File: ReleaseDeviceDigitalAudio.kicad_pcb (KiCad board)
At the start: 2 copper layers, 132.1 x 67.9 mm, 2 parts, among them J3 Conn_02x15_Odd_Even, J9 Conn_02x08_Odd_Even

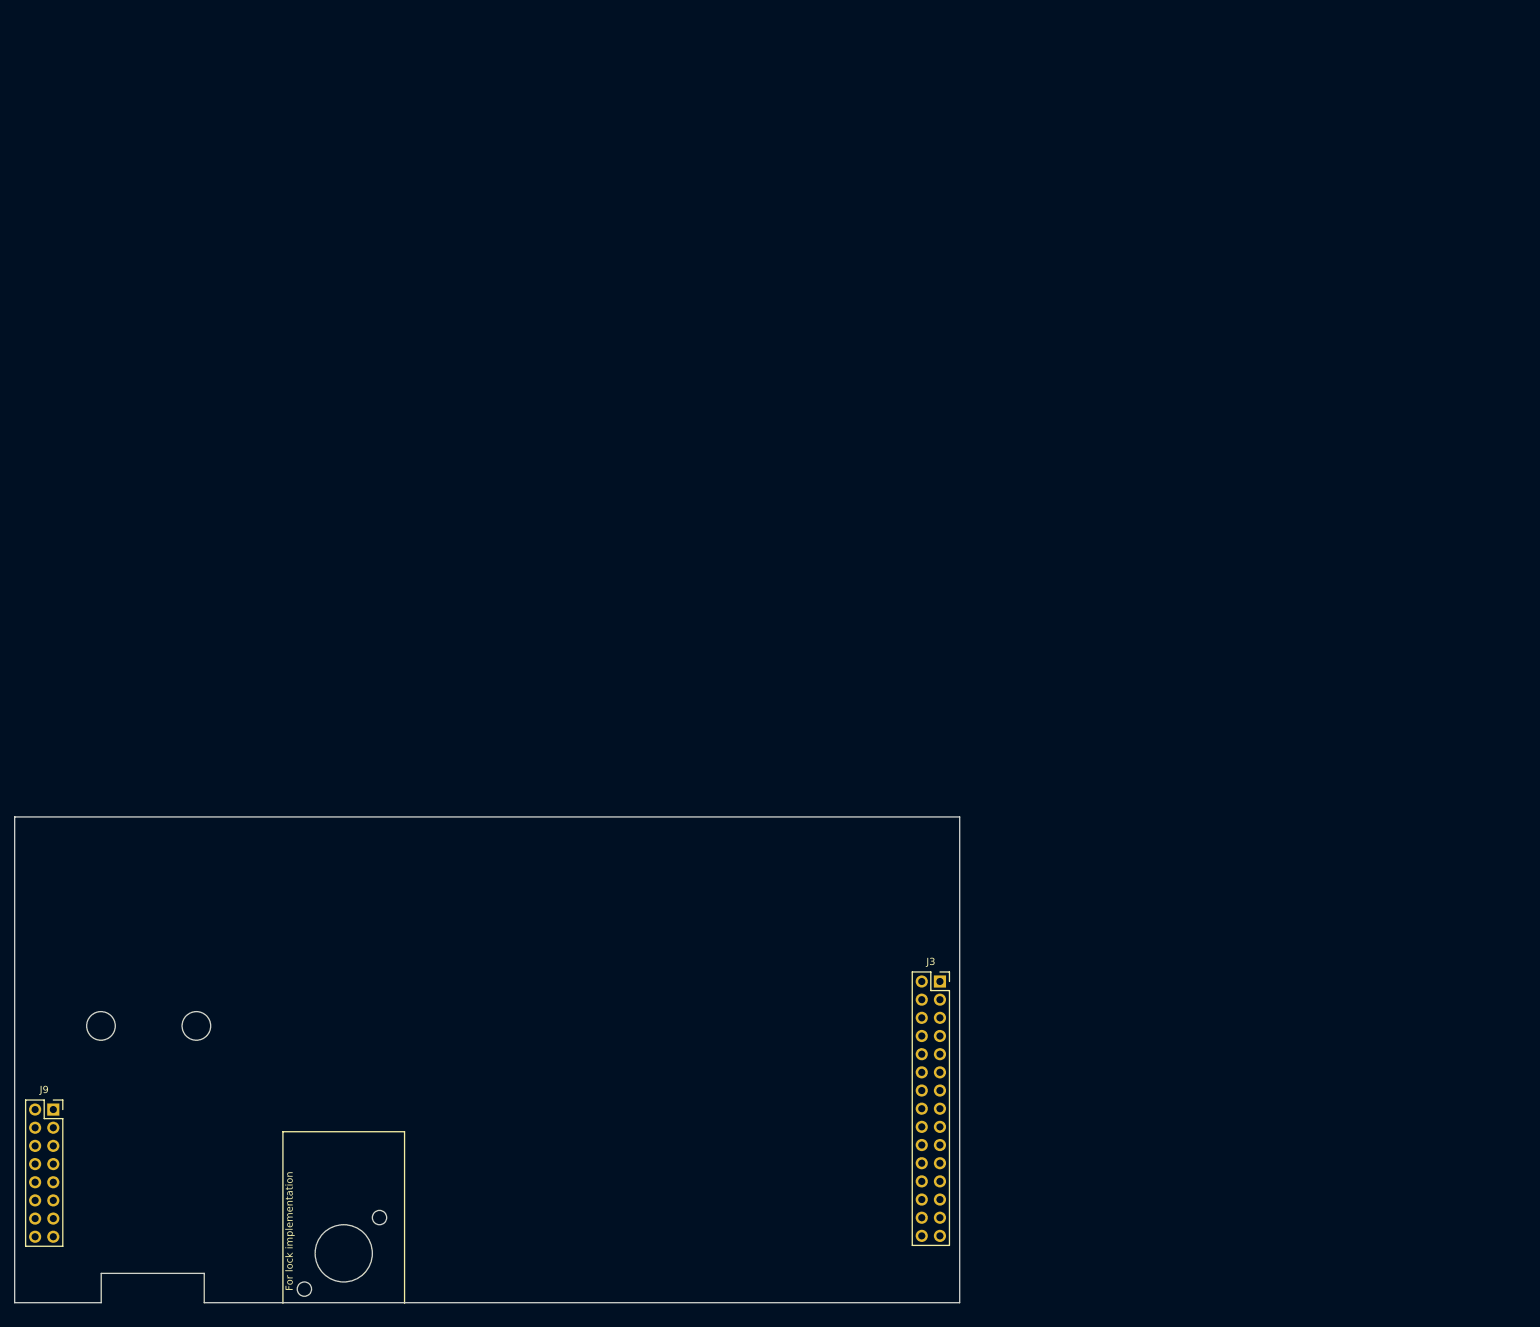
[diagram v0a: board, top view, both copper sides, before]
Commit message: - CM3 durch CM4 ersetzt - Spannungsregler für 3,3 und 1,8V entfernt, da nun von CM4 erzeugt - RTC IC getauscht
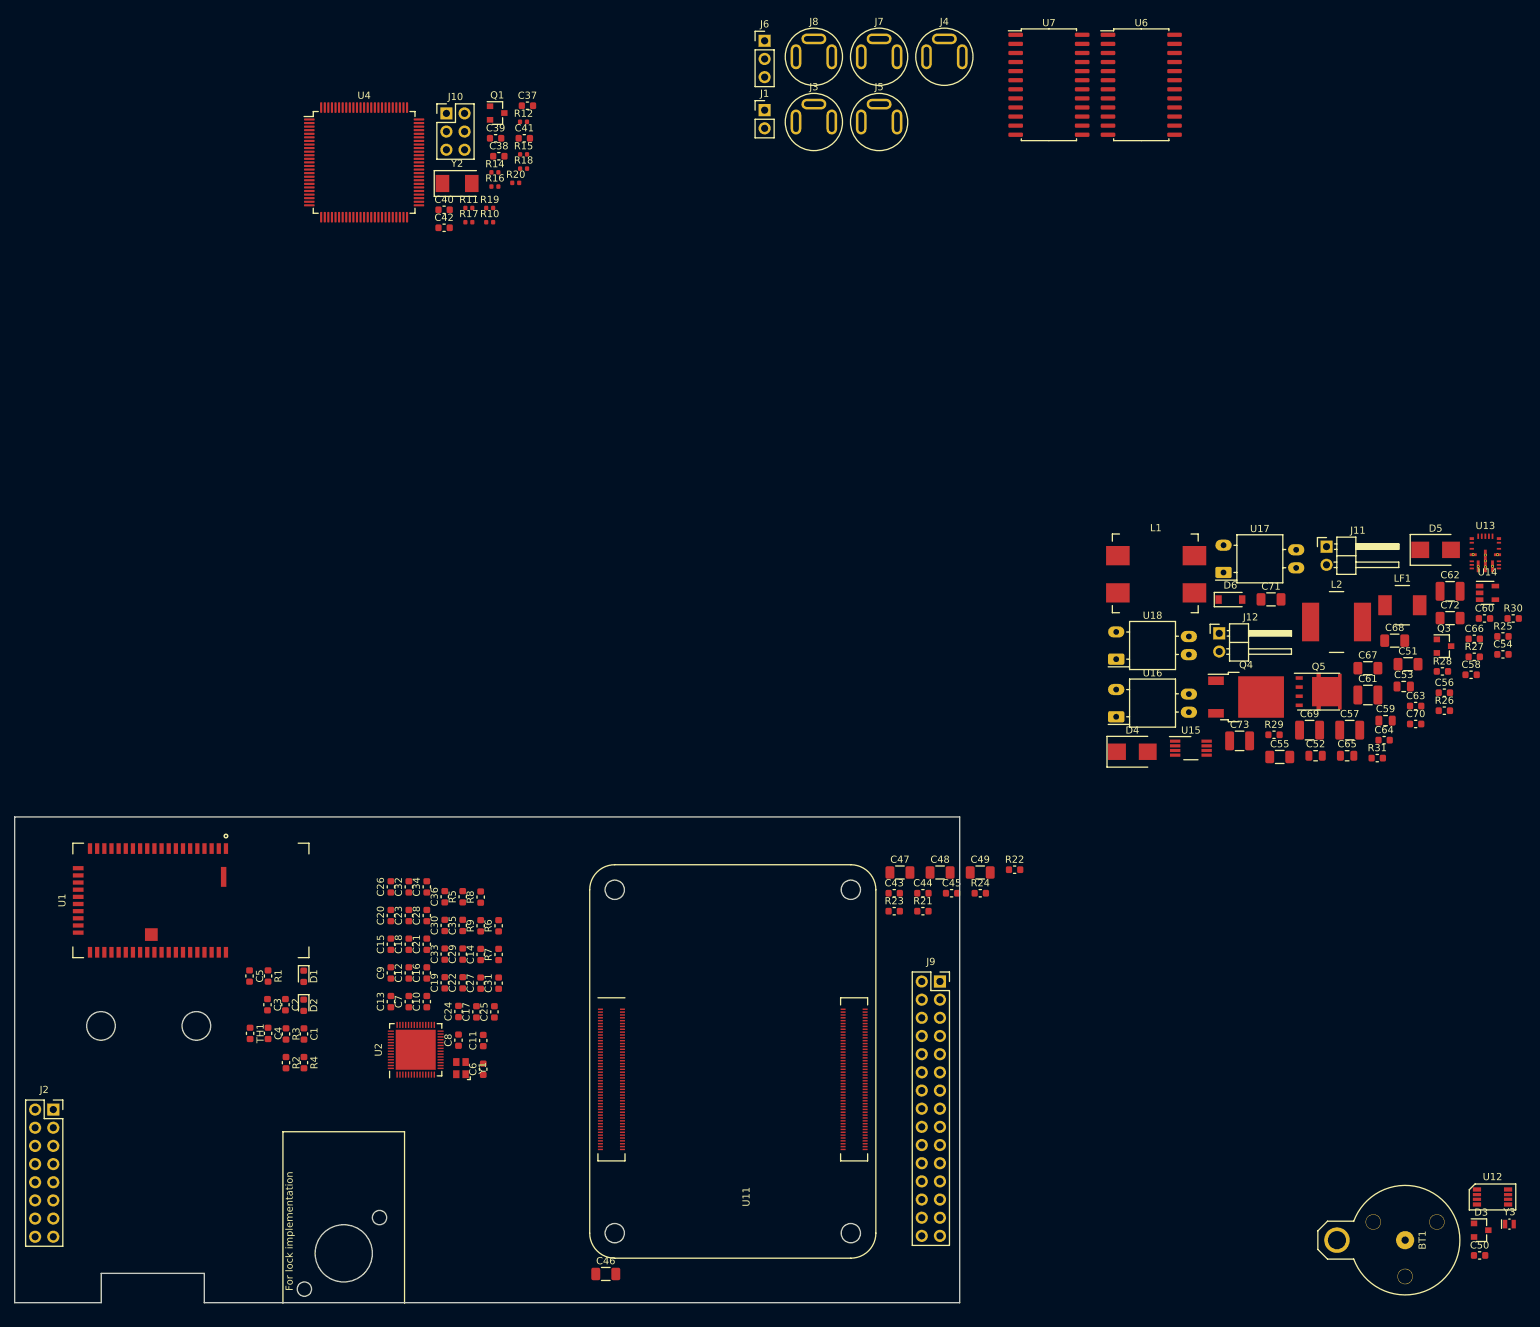
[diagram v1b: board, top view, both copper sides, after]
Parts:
- added BT1: Battery, TeKaDeConn:CR1220, F.Cu at (235.6, 122.7)
- added C1: 1u/16V, Capacitor_SMD:C_0603_1608Metric, F.Cu at (91.2, 93.8)
- added C10: 1u/6V3/X5R, Resistor_SMD:R_0603_1608Metric, F.Cu at (108.4, 89.3)
- added C11: 10p/50V/C0G, Resistor_SMD:R_0603_1608Metric, F.Cu at (116.3, 94.8)
- added C12: 10p/50V/C0G, Resistor_SMD:R_0603_1608Metric, F.Cu at (105.9, 85.3)
- added C13: 1u/6V3/X5R, Resistor_SMD:R_0603_1608Metric, F.Cu at (103.4, 89.3)
- added C14: 1u/6V3/X5R, Resistor_SMD:R_0603_1608Metric, F.Cu at (115.9, 82.7)
- added C15: 10p/50V/C0G, Resistor_SMD:R_0603_1608Metric, F.Cu at (103.4, 81.3)
- added C16: 10p/50V/C0G, Resistor_SMD:R_0603_1608Metric, F.Cu at (108.4, 85.3)
- added C17: 1u/6V3/X5R, Resistor_SMD:R_0603_1608Metric, F.Cu at (115.4, 90.7)
- added C18: 1u/6V3/X5R, Resistor_SMD:R_0603_1608Metric, F.Cu at (105.9, 81.3)
- added C19: 1u/6V3/X5R, Resistor_SMD:R_0603_1608Metric, F.Cu at (110.9, 86.7)
- added C2: 100n/16V/X7R, Capacitor_SMD:C_0603_1608Metric, F.Cu at (88.6, 89.7)
- added C20: 10p/50V/C0G, Resistor_SMD:R_0603_1608Metric, F.Cu at (103.4, 77.3)
- added C21: 10p/50V/C0G, Resistor_SMD:R_0603_1608Metric, F.Cu at (108.4, 81.3)
- added C22: 1u/6V3/X5R, Resistor_SMD:R_0603_1608Metric, F.Cu at (113.4, 86.7)
- added C23: 100n/10V/X7R, Resistor_SMD:R_0603_1608Metric, F.Cu at (105.9, 77.3)
- added C24: 1u/6V3/X5R, Resistor_SMD:R_0603_1608Metric, F.Cu at (112.8, 90.7)
- added C25: 1u/6V3/X5R, Resistor_SMD:R_0603_1608Metric, F.Cu at (117.9, 90.7)
- added C26: 10p/50V/C0G, Resistor_SMD:R_0603_1608Metric, F.Cu at (103.4, 73.3)
- added C27: 10p/50V/C0G, Resistor_SMD:R_0603_1608Metric, F.Cu at (115.9, 86.7)
- added C28: 1u/6V3/X5R, Resistor_SMD:R_0603_1608Metric, F.Cu at (108.4, 77.3)
- added C29: 2u2/6V3/X5R, Resistor_SMD:R_0603_1608Metric, F.Cu at (113.4, 82.7)
- added C3: 100n/16V/X7R, Capacitor_SMD:C_0603_1608Metric, F.Cu at (86.1, 89.7)
- added C30: 1u/6V3/X5R, Resistor_SMD:R_0603_1608Metric, F.Cu at (110.9, 78.7)
- added C31: 1u/6V3/X5R, Resistor_SMD:R_0603_1608Metric, F.Cu at (118.5, 86.7)
- added C32: 10p/50V/C0G, Resistor_SMD:R_0603_1608Metric, F.Cu at (105.9, 73.3)
- added C33: 1u/6V3/X5R, Resistor_SMD:R_0603_1608Metric, F.Cu at (110.9, 82.7)
- added C34: 1u/6V3/X5R, Resistor_SMD:R_0603_1608Metric, F.Cu at (108.4, 73.3)
- added C35: 10p/50V/C0G, Resistor_SMD:R_0603_1608Metric, F.Cu at (113.4, 78.7)
- added C36: 1u/6V3/X5R, Resistor_SMD:R_0603_1608Metric, F.Cu at (110.9, 74.7)
- added C37: 22pF, Capacitor_SMD:C_0603_1608Metric, F.Cu at (122.5, -35.9)
- added C38: 22pF, Capacitor_SMD:C_0603_1608Metric, F.Cu at (118.5, -28.9)
- added C39: 100nF, Capacitor_SMD:C_0603_1608Metric, F.Cu at (118.0, -31.4)
- added C4: 1u/16V, Capacitor_SMD:C_0603_1608Metric, F.Cu at (86.2, 93.8)
- added C40: 100n, Capacitor_SMD:C_0603_1608Metric, F.Cu at (110.8, -21.4)
- added C41: 100n, Capacitor_SMD:C_0603_1608Metric, F.Cu at (122.0, -31.4)
- added C42: 100n, Capacitor_SMD:C_0603_1608Metric, F.Cu at (110.8, -18.9)
- added C43: 100n/16V/X5R, Capacitor_SMD:C_0603_1608Metric, F.Cu at (173.7, 74.2)
- added C44: 100n/16V/X5R, Capacitor_SMD:C_0603_1608Metric, F.Cu at (177.8, 74.2)
- added C45: 100n/16V/X5R, Capacitor_SMD:C_0603_1608Metric, F.Cu at (181.8, 74.2)
- added C46: 47u/10V/X5R, Capacitor_SMD:C_1206_3216Metric, F.Cu at (133.4, 127.4)
- added C47: 22u/6V3/X5R, Capacitor_SMD:C_1206_3216Metric, F.Cu at (174.5, 71.3)
- added C48: 22u/6V3/X5R, Capacitor_SMD:C_1206_3216Metric, F.Cu at (180.2, 71.3)
- added C49: 47u/10V/X5R, Capacitor_SMD:C_1206_3216Metric, F.Cu at (185.8, 71.3)
- added C5: 100n/16V/X7R, Capacitor_SMD:C_0603_1608Metric, F.Cu at (83.6, 85.7)
- added C50: 100n/16V/X5R, Capacitor_SMD:C_0603_1608Metric, F.Cu at (255.6, 124.8)
- added C51: 10u/50V/X5R, Capacitor_SMD:C_1206_3216Metric, F.Cu at (245.6, 42.1)
- added C52: 4n7/100V/X7R, Capacitor_SMD:C_0805_2012Metric, F.Cu at (232.6, 54.9)
- added C53: 4n7/100V/X7R, Capacitor_SMD:C_0805_2012Metric, F.Cu at (245.0, 45.3)
- added C54: 47n/50V/X7R, Capacitor_SMD:C_0603_1608Metric, F.Cu at (258.8, 40.8)
- added C55: 10u/50V/X5R, Capacitor_SMD:C_1206_3216Metric, F.Cu at (227.6, 55.1)
- added C56: 47n/50V/X7R, Capacitor_SMD:C_0603_1608Metric, F.Cu at (250.6, 46.1)
- added C57: 10u/50V/X7R, Capacitor_SMD:C_1210_3225Metric, F.Cu at (237.4, 51.4)
- added C58: 1n/100V/X7R, Capacitor_SMD:C_0603_1608Metric, F.Cu at (254.4, 43.6)
- added C59: 4u7/16V/X7R, Capacitor_SMD:C_0805_2012Metric, F.Cu at (242.4, 50.0)
- added C6: 10u/6V3/X5R, Resistor_SMD:R_0603_1608Metric, F.Cu at (116.3, 98.8)
- added C60: 1n/100V/X7R, Capacitor_SMD:C_0603_1608Metric, F.Cu at (256.3, 35.8)
- added C61: 10u/50V/X7R, Capacitor_SMD:C_1210_3225Metric, F.Cu at (240.0, 46.5)
- added C62: 10u/50V/X7R, Capacitor_SMD:C_1210_3225Metric, F.Cu at (251.4, 32.0)
- added C63: 470n/25V/X5R, Capacitor_SMD:C_0603_1608Metric, F.Cu at (246.6, 48.0)
- added C64: 100n/16V/X7R, Capacitor_SMD:C_0603_1608Metric, F.Cu at (242.2, 52.8)
- added C65: 2u2/50V/X5R, Capacitor_SMD:C_0805_2012Metric, F.Cu at (237.1, 54.9)
- added C66: 100n/16V/X7R, Capacitor_SMD:C_0603_1608Metric, F.Cu at (254.8, 38.6)
- added C67: 22u/10V/X7R, Capacitor_SMD:C_1206_3216Metric, F.Cu at (240.0, 42.7)
- added C68: 22u/10V/X7R, Capacitor_SMD:C_1206_3216Metric, F.Cu at (243.7, 38.9)
- added C69: 47u/10V/X7R, Capacitor_SMD:C_1210_3225Metric, F.Cu at (231.8, 51.4)
- added C7: 100n/10V/X7R, Resistor_SMD:R_0603_1608Metric, F.Cu at (105.9, 89.3)
- added C70: 1n/100V/X7R, Capacitor_SMD:C_0603_1608Metric, F.Cu at (246.6, 50.5)
- added C71: 4u7/50V/X7R, Capacitor_SMD:C_1206_3216Metric, F.Cu at (226.4, 33.1)
- added C72: 4u7/50V/X7R, Capacitor_SMD:C_1206_3216Metric, F.Cu at (251.4, 35.7)
- added C73: 10u/50V/X7R, Capacitor_SMD:C_1210_3225Metric, F.Cu at (222.0, 52.9)
- added C8: 1u/6V3/X5R, Resistor_SMD:R_0603_1608Metric, F.Cu at (112.8, 94.7)
- added C9: 1u/6V3/X5R, Resistor_SMD:R_0603_1608Metric, F.Cu at (103.4, 85.3)
- added D1: LED_BLUE, LED_SMD:LED_0603_1608Metric, F.Cu at (91.2, 85.8)
- added D2: LED_RED, LED_SMD:LED_0603_1608Metric, F.Cu at (91.2, 89.8)
- added D3: BAT54C, Package_TO_SOT_SMD:SOT-23, F.Cu at (255.8, 121.3)
- added D4: SMBJ28A-13-F, Diode_SMD:D_SMB, F.Cu at (207.0, 54.4)
- added D5: SMBJ14A-13-F, Diode_SMD:D_SMB, F.Cu at (249.4, 26.2)
- added D6: MMSZ5245B-7-F, Diode_SMD:D_SOD-123, F.Cu at (220.7, 33.1)
- added J1: Conn_02x01, Connector_PinHeader_2.54mm:PinHeader_1x02_P2.54mm_Vertical, F.Cu at (155.6, -35.3)
- added J10: ATMEGA_ICSP, Connector_PinHeader_2.54mm:PinHeader_2x03_P2.54mm_Vertical, F.Cu at (111.1, -34.8)
- added J11: BAT, Connector_PinHeader_2.54mm:PinHeader_1x02_P2.54mm_Horizontal, F.Cu at (234.2, 25.7)
- added J12: IGNITION, Connector_PinHeader_2.54mm:PinHeader_1x02_P2.54mm_Horizontal, F.Cu at (219.2, 37.8)
- added J3: AudioJack3, TeKaDe:LumbergKLB4, F.Cu at (162.5, -33.6)
- added J4: AudioJack3, TeKaDe:LumbergKLB4, F.Cu at (180.8, -42.8)
- added J5: AudioJack3, TeKaDe:LumbergKLB4, F.Cu at (171.6, -33.6)
- added J6: Conn_01x03_Male, Connector_PinHeader_2.54mm:PinHeader_1x03_P2.54mm_Vertical, F.Cu at (155.6, -45.0)
- added J7: AudioJack3, TeKaDe:LumbergKLB4, F.Cu at (171.6, -42.8)
- added J8: AudioJack3, TeKaDe:LumbergKLB4, F.Cu at (162.5, -42.8)
- added L1: ACM1211-102-2PL-TL01, TeKaDe:ACM1211, F.Cu at (210.2, 29.5)
- added L2: IHLP3232DZER2R2M11, TeKaDe:IHLP-3232DZ, F.Cu at (235.6, 36.3)
- added LF1: IHLP2020CZER2R2M11, TeKaDe:IHLP-2020CZ-11, F.Cu at (244.8, 33.9)
- added Q1: BSS138, Package_TO_SOT_SMD:SOT-23, F.Cu at (118.2, -34.9)
- added Q3: SQ2362ES-T1_GE3, Package_TO_SOT_SMD:SOT-23, F.Cu at (250.6, 39.6)
- added Q4: SQD50P06-15L_GE3, Package_TO_SOT_SMD:TO-252-2, F.Cu at (222.9, 46.7)
- added Q5: SQJ461EP-T1-GE3, TeKaDe:PowerPAK-SO-8L-SINGLE, F.Cu at (233.1, 46.0)
- added R1: 10k/5%, Resistor_SMD:R_0603_1608Metric, F.Cu at (86.2, 85.7)
- added R10: 1M, Resistor_SMD:R_0402_1005Metric, F.Cu at (117.2, -19.6)
- added R11: 100k, Resistor_SMD:R_0402_1005Metric, F.Cu at (114.3, -21.6)
- added R12: 10k, Resistor_SMD:R_0402_1005Metric, F.Cu at (121.9, -33.7)
- added R14: 22k, Resistor_SMD:R_0402_1005Metric, F.Cu at (117.9, -26.6)
- added R15: 22k, Resistor_SMD:R_0402_1005Metric, F.Cu at (121.9, -29.1)
- added R16: 22k, Resistor_SMD:R_0402_1005Metric, F.Cu at (117.9, -24.6)
- added R17: 22k, Resistor_SMD:R_0402_1005Metric, F.Cu at (114.3, -19.6)
- added R18: 22k, Resistor_SMD:R_0402_1005Metric, F.Cu at (121.9, -27.1)
- added R19: 22k, Resistor_SMD:R_0402_1005Metric, F.Cu at (117.2, -21.6)
- added R2: 4k7/1%, Resistor_SMD:R_0603_1608Metric, F.Cu at (88.7, 97.8)
- added R20: 22k, Resistor_SMD:R_0402_1005Metric, F.Cu at (120.8, -25.1)
- added R21: NA, Resistor_SMD:R_0603_1608Metric, F.Cu at (177.8, 76.7)
- added R22: 4k7/1%, Resistor_SMD:R_0603_1608Metric, F.Cu at (190.6, 70.9)
- added R23: NA, Resistor_SMD:R_0603_1608Metric, F.Cu at (173.7, 76.7)
- added R24: 4k7/1%, Resistor_SMD:R_0603_1608Metric, F.Cu at (185.8, 74.2)
- added R25: 100k/5%, Resistor_SMD:R_0603_1608Metric, F.Cu at (258.8, 38.3)
- added R26: 30k1/1%, Resistor_SMD:R_0603_1608Metric, F.Cu at (250.6, 48.6)
- added R27: 2k/1%, Resistor_SMD:R_0603_1608Metric, F.Cu at (254.8, 41.1)
- added R28: 20k/1%, Resistor_SMD:R_0603_1608Metric, F.Cu at (250.4, 43.2)
- added R29: 100k/1%, Resistor_SMD:R_0603_1608Metric, F.Cu at (226.8, 52.0)
- added R3: 1M/1%, Resistor_SMD:R_0603_1608Metric, F.Cu at (88.7, 93.8)
- added R30: 100k/1%, Resistor_SMD:R_0603_1608Metric, F.Cu at (260.3, 35.8)
- added R31: 20k/5%, Resistor_SMD:R_0603_1608Metric, F.Cu at (241.3, 55.3)
- added R4: 86k6/1%, Resistor_SMD:R_0603_1608Metric, F.Cu at (91.2, 97.8)
- added R5: 2k2/1%, Resistor_SMD:R_0603_1608Metric, F.Cu at (113.4, 74.7)
- added R6: 2k2/1%, Resistor_SMD:R_0603_1608Metric, F.Cu at (118.5, 78.7)
- added R7: 2k2/1%, Resistor_SMD:R_0603_1608Metric, F.Cu at (118.5, 82.7)
- added R8: 2k2/1%, Resistor_SMD:R_0603_1608Metric, F.Cu at (115.9, 74.7)
- added R9: 10k/5%, Resistor_SMD:R_0603_1608Metric, F.Cu at (115.9, 78.7)
- added TH1: NTC/100k/1%/4250–4299K, Resistor_SMD:R_0603_1608Metric, F.Cu at (83.7, 93.8)
- added U1: BM83SM1-00TA, TeKaDe:BM83SM1, F.Cu at (75.4, 75.2)
- added U11: Compute_Module_4_Connectors, TeKaDe:Raspberry-Pi-4-Compute-Module, F.Cu at (151.2, 100.2)
- added U12: PCF85063A, TeKaDe:SOT505-1, F.Cu at (257.4, 116.6)
- added U13: LM53635LQRNL*Q1, TeKaDe:TI-VQFN-HR, F.Cu at (256.4, 26.6)
- added U14: TLVH431AQDBVRQ1, Package_TO_SOT_SMD:SOT-23-5, F.Cu at (256.7, 32.2)
- added U15: LM74610-Q1, Package_SO:VSSOP-8_3.0x3.0mm_P0.65mm, F.Cu at (215.2, 53.9)
- added U16: NSL-32, OptoDevice:Luna_NSL-32, F.Cu at (204.8, 49.5)
- added U17: NSL-32, OptoDevice:Luna_NSL-32, F.Cu at (219.8, 29.3)
- added U18: NSL-32, OptoDevice:Luna_NSL-32, F.Cu at (204.8, 41.4)
- added U2: MAX98089ETN+, TeKaDe:QFN-56_EP_7x7_Pitch0.4mm, F.Cu at (106.9, 96.0)
- added U4: ATmega2560-16AU, Package_QFP:TQFP-100_14x14mm_P0.5mm, F.Cu at (99.6, -28.0)
- added U6: CD4514, Package_SO:SOIC-24W_7.5x15.4mm_P1.27mm, F.Cu at (208.3, -38.8)
- added U7: CD4511, Package_SO:SOIC-24W_7.5x15.4mm_P1.27mm, F.Cu at (195.4, -38.8)
- added Y1: 830208220101, TeKaDe:WE_IQXO-791, F.Cu at (113.2, 98.6)
- added Y2: 16MHz, Crystal:Crystal_SMD_Abracon_ABM3-2Pin_5.0x3.2mm, F.Cu at (112.6, -25.0)
- added Y3: 9HT12, Crystal:Crystal_SMD_MicroCrystal_CM9V-T1A-2Pin_1.6x1.0mm, F.Cu at (259.7, 120.4)
- renumbered J9 to J2, J3 to J9
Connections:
- net /Digit19Cathode renamed Net-(J9-Pad10)
- net /PinlineGND renamed Net-(J9-Pad28)
- net /PinlineVcc renamed Net-(J9-Pad30)
- net /SegmentFAnode5 renamed /Digit5Cathode
- J2 pad 1: /LedYellowCathode -> /UiLdr
- J2 pad 10: /DataEncoderDataOutC -> /DataEncoderDataOutB
- J2 pad 11: +5V -> /DataEncoderDataOutA
- J2 pad 12: /DataEncoderDataOutA -> +5V
- J2 pad 13: /OnSwitchLedAnode -> GND
- J2 pad 14: Earth -> /OnSwitchLedAnode
- J2 pad 15: /DataEncoderDataOutD -> /DataEncoderDataOutE
- J2 pad 16: /DataEncoderDataOutE -> /DataEncoderDataOutD
- J2 pad 2: /UiLdr -> /LedYellowCathode
- J2 pad 3: /LedRedCathode -> /LedGreenCathode
- J2 pad 4: /LedGreenCathode -> /LedRedCathode
- J2 pad 5: /ButtonA2GND -> Net-(J2-Pad5)
- J2 pad 6: /PINLINE_RIGHT_6 -> /ButtonA2GND
- J2 pad 7: /DataEncoderOutputEnable -> /DataEncoderDataAvailable
- J2 pad 8: /DataEncoderDataAvailable -> /DataEncoderOutputEnable
- J2 pad 9: /DataEncoderDataOutB -> /DataEncoderDataOutC
- J9 pad 1: /SegmentEAnode -> /SegmentFAnode
- J9 pad 11: /Digit12Cathode -> /Digit8Cathode
- J9 pad 12: /Digit13Cathode -> /Digit7Cathode
- J9 pad 13: /Digit14Cathode -> /Digit10Cathode
- J9 pad 14: /Digit15Cathode -> /Digit9Cathode
- J9 pad 15: /Digit16Cathode -> /Digit12Cathode
- J9 pad 16: /Digit17Cathode -> /Digit11Cathode
- J9 pad 17: /Digit18Cathode -> /Digit6Cathode
- J9 pad 18: /Digit11Cathode -> /Digit13Cathode
- J9 pad 19: /Digit3Cathode -> /DigitACathode
- J9 pad 2: /SegmentFAnode -> /SegmentEAnode
- J9 pad 20: /Digit2Cathode -> /DigitBCathode
- J9 pad 21: /Digit7Cathode -> /Digit1Cathode
- J9 pad 22: /Digit6Cathode -> /Digit2Cathode
- J9 pad 23: /Digit9Cathode -> /Digit3Cathode
- J9 pad 24: /Digit8Cathode -> /Digit4Cathode
- J9 pad 26: /Digit6Cathode -> Net-(J9-Pad26)
- J9 pad 27: /SegmentFAnode7 -> GND
- J9 pad 29: /SegmentFAnode9 -> +5V
- J9 pad 3: /SegmentAAnode -> /SegmentBAnode
- J9 pad 4: /SegmentBAnode -> /SegmentAAnode
- J9 pad 5: /SegmentDAnode -> /SegmentGAnode
- J9 pad 6: /SegmentGAnode -> /SegmentDAnode
- J9 pad 7: /SegmentCAnode -> Net-(J9-Pad7)
- J9 pad 8: /Digit21Cathode -> /SegmentCAnode
- J9 pad 9: /Digit20Cathode -> /Digit14Cathode

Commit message: - Outline / Postionierung Zwischenstand
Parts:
- removed the C2 at (88.6, 89.7)
- removed the C37 at (122.5, -35.9)
- removed the C38 at (118.5, -28.9)
- removed the C39 at (118.0, -31.4)
- removed the C44 at (177.8, 74.2)
- removed the C5 at (83.6, 85.7)
- removed the J1 at (155.6, -35.3)
- removed the J2 at (56.2, 104.4)
- removed Q1: BSS138, Package_TO_SOT_SMD:SOT-23
- removed Q5: SQJ461EP-T1-GE3, TeKaDe:PowerPAK-SO-8L-SINGLE
- removed the R12 at (121.9, -33.7)
- removed the R14 at (117.9, -26.6)
- removed the R15 at (121.9, -29.1)
- removed U16, U17, U18: NSL-32, OptoDevice:Luna_NSL-32
- removed the U6 at (208.3, -38.8)
- removed the Y2 at (112.6, -25.0)
- added C3: 100n/16V/X7R, Capacitor_SMD:C_0402_1005Metric, F.Cu at (87.8, 47.5)
- added C43: 100n/16V/X7R, Capacitor_SMD:C_0402_1005Metric, F.Cu at (249.3, 102.4)
- added C46: 100n/16V/X7R, Capacitor_SMD:C_0402_1005Metric, F.Cu at (250.8, 55.7)
- added C6: 100n/16V/X7R, Capacitor_SMD:C_0402_1005Metric, F.Cu at (84.9, 47.5)
- added C7: 100n/16V/X7R, Capacitor_SMD:C_0402_1005Metric, F.Cu at (50.6, 127.4)
- added C74: 4u7/50V/X7R, Capacitor_SMD:C_1206_3216Metric, F.Cu at (40.4, 163.6)
- added C75: 4u7/50V/X7R, Capacitor_SMD:C_1206_3216Metric, F.Cu at (65.4, 166.2)
- added C76: 10u/50V/X7R, Capacitor_SMD:C_1210_3225Metric, F.Cu at (36.0, 183.4)
- added C77: 4u7/16V/X7R, Capacitor_SMD:C_0805_2012Metric, F.Cu at (39.2, 118.5)
- added C79: 100n/16V/X7R, Capacitor_SMD:C_0402_1005Metric, F.Cu at (55.9, 111.5)
- added C8: 100n/16V/X7R, Capacitor_SMD:C_0402_1005Metric, F.Cu at (53.5, 127.4)
- added C80: 100n/16V/X7R, Capacitor_SMD:C_0402_1005Metric, F.Cu at (50.0, 116.4)
- added D10: 1N4148WQ-7-F, Diode_SMD:D_SOD-123F, F.Cu at (149.2, 186.8)
- added D11: MMSZ5245B-7-F, Diode_SMD:D_SOD-123, F.Cu at (34.7, 163.6)
- added D7: SMBJ28A-13-F, Diode_SMD:D_SMB, F.Cu at (150.6, 176.8)
- added D8: SMBJ14A-13-F, Diode_SMD:D_SMB, F.Cu at (150.6, 182.3)
- added D9: 1N4148WQ-7-F, Diode_SMD:D_SOD-123F, F.Cu at (140.7, 187.0)
- added H1: MountingHole, MountingHole:MountingHole_3.2mm_M3_DIN965, F.Cu at (87.0, 126.5)
- added H2: MountingHole, MountingHole:MountingHole_3.2mm_M3_DIN965, F.Cu at (87.0, 79.5)
- added H3: MountingHole, MountingHole:MountingHole_3.2mm_M3_DIN965, F.Cu at (213.0, 126.5)
- added H4: MountingHole, MountingHole:MountingHole_3.2mm_M3_DIN965, F.Cu at (213.0, 79.5)
- added H5: MountingHole, MountingHole:MountingHole_4mm, F.Cu at (108.5, 91.0)
- added H6: MountingHole, MountingHole:MountingHole_4mm, F.Cu at (96.5, 91.0)
- added H7: MountingHole, MountingHole:MountingHole_2.5mm, F.Cu at (135.0, 117.5)
- added H8: MountingHole, MountingHole:MountingHole_2.5mm, F.Cu at (125.0, 127.5)
- added H9: MountingHole, MountingHole:MountingHole_8.4mm_M8, F.Cu at (130.0, 122.5)
- added IC1: ULN2003F12FN-7, TeKaDe:U-DFN3030-10, F.Cu at (258.9, 97.1)
- added IC2: ULN2003F12FN-7, TeKaDe:U-DFN3030-10, F.Cu at (254.8, 97.1)
- added IC3: ULN2003F12FN-7, TeKaDe:U-DFN3030-10, F.Cu at (254.8, 101.7)
- added IC4: ULN2003F12FN-7, TeKaDe:U-DFN3030-10, F.Cu at (263.0, 97.1)
- added J7: BAT, Connector_PinHeader_2.54mm:PinHeader_1x02_P2.54mm_Horizontal, F.Cu at (48.2, 156.2)
- added J8: IGNITION, Connector_PinHeader_2.54mm:PinHeader_1x02_P2.54mm_Horizontal, F.Cu at (33.2, 168.3)
- added L3: Ferrit/470R/1A/0,2R, Inductor_SMD:L_0603_1608Metric, F.Cu at (43.5, 123.7)
- added Q2: SQ2362ES-T1_GE3, Package_TO_SOT_SMD:SOT-23, F.Cu at (64.6, 170.1)
- added R21: 2k2/5%/250mW, Resistor_SMD:R_0603_1608Metric, F.Cu at (161.2, 179.5)
- added R22: 100k/5%, Resistor_SMD:R_0402_1005Metric, F.Cu at (72.8, 168.8)
- added R23: 10k/1%, Resistor_SMD:R_0402_1005Metric, F.Cu at (161.9, 175.0)
- added R24: 10k/1%, Resistor_SMD:R_0402_1005Metric, F.Cu at (144.9, 186.3)
- added R32: 20k/5%, Resistor_SMD:R_0402_1005Metric, F.Cu at (55.3, 185.8)
- added R33: 392R/1%, Resistor_SMD:R_0805_2012Metric, F.Cu at (39.2, 121.5)
- added R34: 392R/1%, Resistor_SMD:R_0805_2012Metric, F.Cu at (50.8, 110.0)
- added R35: 392R/1%, Resistor_SMD:R_0805_2012Metric, F.Cu at (50.8, 107.0)
- added R36: 10k/1%, Resistor_SMD:R_0603_1608Metric, F.Cu at (34.4, 128.0)
- added R37: 392R/1%, Resistor_SMD:R_0805_2012Metric, F.Cu at (55.2, 107.0)
- added R38: 22k/1%, Resistor_SMD:R_0402_1005Metric, F.Cu at (37.9, 127.8)
- added R39: 22k/1%, Resistor_SMD:R_0402_1005Metric, F.Cu at (38.5, 124.0)
- added R40: 22k/1%, Resistor_SMD:R_0402_1005Metric, F.Cu at (54.5, 109.5)
- added R41: 22k/1%, Resistor_SMD:R_0402_1005Metric, F.Cu at (50.0, 112.4)
- added R42: 22k/1%, Resistor_SMD:R_0402_1005Metric, F.Cu at (58.9, 106.5)
- added R43: 22k/1%, Resistor_SMD:R_0402_1005Metric, F.Cu at (53.0, 112.4)
- added R44: 100k/5%, Resistor_SMD:R_0402_1005Metric, F.Cu at (50.0, 114.4)
- added R45: 22k/1%, Resistor_SMD:R_0402_1005Metric, F.Cu at (41.4, 125.9)
- added R46: 15k, Resistor_SMD:R_0402_1005Metric, F.Cu at (53.0, 114.4)
- added TP1: CM4PWR, TestPoint:TestPoint_Pad_D1.5mm, F.Cu at (252.2, 52.9)
- added U10: VOMA617A, Package_SO:SOP-4_3.8x4.1mm_P2.54mm, F.Cu at (142.2, 176.8)
- added U11: VOMA617A, Package_SO:SOP-4_3.8x4.1mm_P2.54mm, F.Cu at (142.2, 182.5)
- added U12: LM53635LQRNL*Q1, TeKaDe:TI-VQFN-HR, F.Cu at (70.4, 157.1)
- added U3: SN74LV1T126, Package_TO_SOT_SMD:SOT-23-5, F.Cu at (56.5, 124.1)
- added U8: CD4511BPWR, Package_SO:TSSOP-14_4.4x5mm_P0.65mm, F.Cu at (248.3, 98.1)
- C1: renamed from C50; value 100n/16V/X5R -> 100n/16V/X7R; footprint Capacitor_SMD:C_0603_1608Metric -> Capacitor_SMD:C_0402_1005Metric
- C10: renamed from C6; footprint Resistor_SMD:R_0603_1608Metric -> Capacitor_SMD:C_0603_1608Metric
- C11: renamed from C7; value 100n/10V/X7R -> 100n/16V/X7R; footprint Resistor_SMD:R_0603_1608Metric -> Capacitor_SMD:C_0402_1005Metric
- C12: renamed from C8; footprint Resistor_SMD:R_0603_1608Metric -> Capacitor_SMD:C_0402_1005Metric
- C13: renamed from C9; footprint Resistor_SMD:R_0603_1608Metric -> Capacitor_SMD:C_0402_1005Metric
- C14: renamed from C10; footprint Resistor_SMD:R_0603_1608Metric -> Capacitor_SMD:C_0402_1005Metric
- C15: renamed from C11; footprint Resistor_SMD:R_0603_1608Metric -> Capacitor_SMD:C_0402_1005Metric
- C16: renamed from C12; footprint Resistor_SMD:R_0603_1608Metric -> Capacitor_SMD:C_0402_1005Metric
- C17: renamed from C13; footprint Resistor_SMD:R_0603_1608Metric -> Capacitor_SMD:C_0402_1005Metric
- C18: renamed from C14; footprint Resistor_SMD:R_0603_1608Metric -> Capacitor_SMD:C_0402_1005Metric
- C19: renamed from C15; footprint Resistor_SMD:R_0603_1608Metric -> Capacitor_SMD:C_0402_1005Metric
- C2: renamed from C1; value 1u/16V -> 1u/6V3/X5R; footprint Capacitor_SMD:C_0603_1608Metric -> Capacitor_SMD:C_0402_1005Metric
- C20: renamed from C16; footprint Resistor_SMD:R_0603_1608Metric -> Capacitor_SMD:C_0402_1005Metric
- C21: renamed from C17; footprint Resistor_SMD:R_0603_1608Metric -> Capacitor_SMD:C_0402_1005Metric
- C22: renamed from C18; footprint Resistor_SMD:R_0603_1608Metric -> Capacitor_SMD:C_0402_1005Metric
- C23: renamed from C19; footprint Resistor_SMD:R_0603_1608Metric -> Capacitor_SMD:C_0402_1005Metric
- C24: renamed from C20; footprint Resistor_SMD:R_0603_1608Metric -> Capacitor_SMD:C_0402_1005Metric
- C25: renamed from C21; footprint Resistor_SMD:R_0603_1608Metric -> Capacitor_SMD:C_0402_1005Metric
- C26: renamed from C22; footprint Resistor_SMD:R_0603_1608Metric -> Capacitor_SMD:C_0402_1005Metric
- C27: renamed from C23; value 100n/10V/X7R -> 100n/16V/X7R; footprint Resistor_SMD:R_0603_1608Metric -> Capacitor_SMD:C_0402_1005Metric
- C28: renamed from C24; footprint Resistor_SMD:R_0603_1608Metric -> Capacitor_SMD:C_0402_1005Metric
- C29: renamed from C25; footprint Resistor_SMD:R_0603_1608Metric -> Capacitor_SMD:C_0402_1005Metric
- C30: renamed from C26; footprint Resistor_SMD:R_0603_1608Metric -> Capacitor_SMD:C_0402_1005Metric
- C31: renamed from C27; footprint Resistor_SMD:R_0603_1608Metric -> Capacitor_SMD:C_0402_1005Metric
- C32: renamed from C28; footprint Resistor_SMD:R_0603_1608Metric -> Capacitor_SMD:C_0402_1005Metric
- C33: renamed from C29; footprint Resistor_SMD:R_0603_1608Metric -> Capacitor_SMD:C_0603_1608Metric
- C34: renamed from C30; footprint Resistor_SMD:R_0603_1608Metric -> Capacitor_SMD:C_0402_1005Metric
- C35: renamed from C31; footprint Resistor_SMD:R_0603_1608Metric -> Capacitor_SMD:C_0402_1005Metric
- C36: renamed from C32; footprint Resistor_SMD:R_0603_1608Metric -> Capacitor_SMD:C_0402_1005Metric
- C37: renamed from C33; footprint Resistor_SMD:R_0603_1608Metric -> Capacitor_SMD:C_0402_1005Metric
- C38: renamed from C34; footprint Resistor_SMD:R_0603_1608Metric -> Capacitor_SMD:C_0402_1005Metric
- C39: renamed from C35; footprint Resistor_SMD:R_0603_1608Metric -> Capacitor_SMD:C_0402_1005Metric
- C4: renamed from C3; footprint Capacitor_SMD:C_0603_1608Metric -> Capacitor_SMD:C_0402_1005Metric
- C40: renamed from C36; footprint Resistor_SMD:R_0603_1608Metric -> Capacitor_SMD:C_0402_1005Metric
- C41: value 100n -> 100n/16V/X7R; footprint Capacitor_SMD:C_0603_1608Metric -> Capacitor_SMD:C_0402_1005Metric
- C42: value 100n -> NA
- C44: renamed from C43; value 100n/16V/X5R -> 100n/16V/X7R; footprint Capacitor_SMD:C_0603_1608Metric -> Capacitor_SMD:C_0402_1005Metric
- C45: value 100n/16V/X5R -> 100n/16V/X7R; footprint Capacitor_SMD:C_0603_1608Metric -> Capacitor_SMD:C_0402_1005Metric
- C48: renamed from C47; footprint Capacitor_SMD:C_1206_3216Metric -> Capacitor_SMD:C_0805_2012Metric
- C49: renamed from C48; footprint Capacitor_SMD:C_1206_3216Metric -> Capacitor_SMD:C_0805_2012Metric
- C5: renamed from C4; value 1u/16V -> 1u/6V3/X5R; footprint Capacitor_SMD:C_0603_1608Metric -> Capacitor_SMD:C_0402_1005Metric
- C54: value 47n/50V/X7R -> 4n7/100V/X7R; footprint Capacitor_SMD:C_0603_1608Metric -> Capacitor_SMD:C_0805_2012Metric
- C55: value 10u/50V/X5R -> 4n7/100V/X7R; footprint Capacitor_SMD:C_1206_3216Metric -> Capacitor_SMD:C_0805_2012Metric
- C57: value 10u/50V/X7R -> 10u/50V/X5R; footprint Capacitor_SMD:C_1210_3225Metric -> Capacitor_SMD:C_1206_3216Metric
- C58: value 1n/100V/X7R -> 47n/50V/X7R
- C59: value 4u7/16V/X7R -> 10u/50V/X7R; footprint Capacitor_SMD:C_0805_2012Metric -> Capacitor_SMD:C_1210_3225Metric
- C60: value 1n/100V/X7R -> 10u/50V/X7R; footprint Capacitor_SMD:C_0603_1608Metric -> Capacitor_SMD:C_1210_3225Metric
- C61, C73: value 10u/50V/X7R -> 1n/100V/X7R; footprint Capacitor_SMD:C_1210_3225Metric -> Capacitor_SMD:C_0603_1608Metric
- C62: value 10u/50V/X7R -> 4u7/16V/X7R; footprint Capacitor_SMD:C_1210_3225Metric -> Capacitor_SMD:C_0805_2012Metric
- C63: value 470n/25V/X5R -> 1n/100V/X7R
- C64: value 100n/16V/X7R -> 10u/50V/X7R; footprint Capacitor_SMD:C_0603_1608Metric -> Capacitor_SMD:C_1210_3225Metric
- C65: value 2u2/50V/X5R -> 10u/50V/X7R; footprint Capacitor_SMD:C_0805_2012Metric -> Capacitor_SMD:C_1210_3225Metric
- C66: value 100n/16V/X7R -> 470n/25V/X5R
- C67: value 22u/10V/X7R -> 100n/16V/X7R; footprint Capacitor_SMD:C_1206_3216Metric -> Capacitor_SMD:C_0402_1005Metric
- C68: value 22u/10V/X7R -> 2u2/50V/X5R; footprint Capacitor_SMD:C_1206_3216Metric -> Capacitor_SMD:C_0805_2012Metric
- C69: value 47u/10V/X7R -> 100n/16V/X7R; footprint Capacitor_SMD:C_1210_3225Metric -> Capacitor_SMD:C_0402_1005Metric
- C70: value 1n/100V/X7R -> 22u/10V/X7R; footprint Capacitor_SMD:C_0603_1608Metric -> Capacitor_SMD:C_0805_2012Metric
- C71: value 4u7/50V/X7R -> 22u/10V/X7R; footprint Capacitor_SMD:C_1206_3216Metric -> Capacitor_SMD:C_0805_2012Metric
- C72: value 4u7/50V/X7R -> 47u/10V/X7R; footprint Capacitor_SMD:C_1206_3216Metric -> Capacitor_SMD:C_1210_3225Metric
- C78: renamed from C40; value 100n -> 100n/16V/X7R; footprint Capacitor_SMD:C_0603_1608Metric -> Capacitor_SMD:C_0402_1005Metric
- D4: value SMBJ28A-13-F -> LED_GRN; footprint Diode_SMD:D_SMB -> LED_SMD:LED_0603_1608Metric
- D5: value SMBJ14A-13-F -> SMBJ28A-13-F
- D6: value MMSZ5245B-7-F -> SMBJ14A-13-F; footprint Diode_SMD:D_SOD-123 -> Diode_SMD:D_SMB
- J10: value ATMEGA_ICSP -> UIBoardCON1; footprint Connector_PinHeader_2.54mm:PinHeader_2x03_P2.54mm_Vertical -> Connector_PinSocket_2.54mm:PinSocket_2x08_P2.54mm_Vertical
- J11: value BAT -> SignalStrength; footprint Connector_PinHeader_2.54mm:PinHeader_1x02_P2.54mm_Horizontal -> Connector_PinHeader_2.54mm:PinHeader_1x02_P2.54mm_Vertical
- J12: value IGNITION -> KeySwitch; footprint Connector_PinHeader_2.54mm:PinHeader_1x02_P2.54mm_Horizontal -> Connector_PinHeader_2.54mm:PinHeader_1x03_P2.54mm_Vertical
- J6: value Conn_01x03_Male -> UIBoardCON2; footprint Connector_PinHeader_2.54mm:PinHeader_1x03_P2.54mm_Vertical -> Connector_PinSocket_2.54mm:PinSocket_2x15_P2.54mm_Vertical
- J9: value Conn_02x15_Odd_Even -> ATMEGA_PROG; footprint Connector_PinSocket_2.54mm:PinSocket_2x15_P2.54mm_Vertical -> Connector_PinHeader_2.54mm:PinHeader_1x03_P2.54mm_Vertical
- Q3: value SQ2362ES-T1_GE3 -> SQD50P06-15L_GE3; footprint Package_TO_SOT_SMD:SOT-23 -> Package_TO_SOT_SMD:TO-252-2
- Q4: value SQD50P06-15L_GE3 -> SQJ461EP-T1-GE3; footprint Package_TO_SOT_SMD:TO-252-2 -> TeKaDe:PowerPAK-SO-8L-SINGLE
- R1, R2, R26, R27, R3, R30, R4, R5, R6, R7, R8, R9: footprint Resistor_SMD:R_0603_1608Metric -> Resistor_SMD:R_0402_1005Metric
- R10: value 1M -> 0R; footprint Resistor_SMD:R_0402_1005Metric -> Resistor_SMD:R_0603_1608Metric
- R11: value 100k -> 1k/1%; footprint Resistor_SMD:R_0402_1005Metric -> Resistor_SMD:R_0603_1608Metric
- R12: renamed from R21; footprint Resistor_SMD:R_0603_1608Metric -> Resistor_SMD:R_0402_1005Metric
- R13: renamed from R22; value 4k7/1% -> NA; footprint Resistor_SMD:R_0603_1608Metric -> Resistor_SMD:R_0402_1005Metric
- R14: renamed from R23; footprint Resistor_SMD:R_0603_1608Metric -> Resistor_SMD:R_0402_1005Metric
- R15: renamed from R24; value 4k7/1% -> NA; footprint Resistor_SMD:R_0603_1608Metric -> Resistor_SMD:R_0402_1005Metric
- R16, R17, R19: value 22k -> NA; footprint Resistor_SMD:R_0402_1005Metric -> Resistor_SMD:R_0603_1608Metric
- R18: value 22k -> 0R; footprint Resistor_SMD:R_0402_1005Metric -> Resistor_SMD:R_0603_1608Metric
- R20: value 22k -> 2k2/5%/250mW; footprint Resistor_SMD:R_0402_1005Metric -> Resistor_SMD:R_0603_1608Metric
- R25: value 100k/5% -> 10k/1%; footprint Resistor_SMD:R_0603_1608Metric -> Resistor_SMD:R_0402_1005Metric
- R28: value 20k/1% -> 10k/1%; footprint Resistor_SMD:R_0603_1608Metric -> Resistor_SMD:R_0402_1005Metric
- R29: value 100k/1% -> 20k/1%; footprint Resistor_SMD:R_0603_1608Metric -> Resistor_SMD:R_0402_1005Metric
- R31: value 20k/5% -> 100k/1%; footprint Resistor_SMD:R_0603_1608Metric -> Resistor_SMD:R_0402_1005Metric
- U13: value LM53635LQRNL*Q1 -> TLVH431AQDBVRQ1; footprint TeKaDe:TI-VQFN-HR -> Package_TO_SOT_SMD:SOT-23-5
- U14: value TLVH431AQDBVRQ1 -> LM74610-Q1; footprint Package_TO_SOT_SMD:SOT-23-5 -> Package_SO:VSSOP-8_3.0x3.0mm_P0.65mm
- U15: value LM74610-Q1 -> ATmega4809-A; footprint Package_SO:VSSOP-8_3.0x3.0mm_P0.65mm -> Package_QFP:TQFP-48_7x7mm_P0.5mm
- U4: value ATmega2560-16AU -> SN74LV1T126; footprint Package_QFP:TQFP-100_14x14mm_P0.5mm -> Package_TO_SOT_SMD:SOT-23-5
- U7: value CD4511 -> CD4514BM
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- renumbered C46 to C47, C49 to C50, D3 to D1, D1 to D2, D2 to D3, J3 to J1, J4 to J2, J5 to J3, J7 to J4, J8 to J5, U12 to U1, U1 to U2, U2 to U6, U11 to U9, Y3 to Y1, Y1 to Y2
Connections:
- net /BM83_MFB renamed /BluetoothModule/BM83_MFB
- net /MAX_IRQ renamed /RPiCM4/GPIO10
- C42 pad 1: +5V -> Net-(C42-Pad1)
- C45 pad 1: +1V8 -> +3V3
- C54 pad 1: VPP -> Net-(C54-Pad1)
- C54 pad 2: GND -> Net-(C54-Pad2)
- C55 pad 1: VPP -> Net-(C54-Pad2)
- C55 pad 2: GND -> -BATT
- C57 pad 1: +BATT -> VPP
- C57 pad 2: -BATT -> GND
- C58 pad 1: -BATT -> VPP
- C58 pad 2: +BATT -> GND
- C59 pad 1: GND -> +BATT
- C59 pad 2: Net-(C59-Pad2) -> -BATT
- C60 pad 1: Net-(C60-Pad1) -> Net-(C54-Pad1)
- C60 pad 2: GND -> -BATT
- C61 pad 1: Net-(C60-Pad1) -> -BATT
- C61 pad 2: GND -> +BATT
- C62 pad 1: Net-(C60-Pad1) -> GND
- C62 pad 2: GND -> Net-(C62-Pad2)
- C63 pad 2: Net-(C63-Pad2) -> GND
- C64 pad 1: +5V -> Net-(C63-Pad1)
- C65 pad 1: Net-(C65-Pad1) -> Net-(C63-Pad1)
- C65 pad 2: Net-(C65-Pad2) -> GND
- C66 pad 1: +5V -> Net-(C66-Pad1)
- C66 pad 2: GND -> Net-(C66-Pad2)
- C68 pad 1: +5V -> Net-(C68-Pad1)
- C68 pad 2: GND -> Net-(C68-Pad2)
- C70 pad 1: Net-(C70-Pad1) -> +5V
- C71 pad 1: Net-(C70-Pad1) -> +5V
- C72 pad 1: Net-(C70-Pad1) -> +5V
- C73 pad 1: VPP -> Net-(C73-Pad1)
- D4 pad 1: +BATT -> Net-(D4-Pad1)
- D4 pad 2: Net-(D4-Pad2) -> +3V3
- D5 pad 1: -BATT -> +BATT
- D5 pad 2: Net-(D4-Pad2) -> Net-(D5-Pad2)
- D6 pad 1: Net-(D6-Pad1) -> -BATT
- D6 pad 2: Net-(D6-Pad2) -> Net-(D5-Pad2)
- J10 pad 1: /ControllerUIBoard/ATMEGA_ICSP_MISO -> /ControllerUIBoard/LDR
- J10 pad 2: +5V -> /ControllerUIBoard/LED_YL
- J10 pad 3: /ControllerUIBoard/ATMEGA_ICSP_SCK -> /ControllerUIBoard/LED_GN
- J10 pad 4: /ControllerUIBoard/ATMEGA_ICSP_MOSI -> /ControllerUIBoard/LED_RD
- J10 pad 5: /ControllerUIBoard/ATMEGA_RESET -> Net-(J10-Pad5)
- J10 pad 6: GND -> /ControllerUIBoard/ButtonA2GND
- J11 pad 1: +BATT -> /ControllerUIBoard/Signal_Strength_Dial_+
- J11 pad 2: -BATT -> GND
- J12 pad 1: Net-(J12-Pad1) -> /ControllerUIBoard/KeySwitchA
- J12 pad 2: -BATT -> /ControllerUIBoard/KeySwitchB
- J6 pad 1: /KeyLock.A -> /7SegmentDriver/SegmentFAnode
- J6 pad 2: /KeyLock.B -> /7SegmentDriver/SegmentEAnode
- J6 pad 3: GND -> /7SegmentDriver/SegmentBAnode
- J9 pad 1: /SegmentFAnode -> +5V
- J9 pad 2: /SegmentEAnode -> /ControllerUIBoard/UPDI_DATA
- J9 pad 3: /SegmentBAnode -> GND
- L1 pad 3: Net-(C60-Pad1) -> Net-(C63-Pad1)
- L2 pad 1: Net-(C63-Pad2) -> Net-(C66-Pad2)
- LF1 pad 1: Net-(C70-Pad1) -> Net-(C73-Pad1)
- Q3 pad 1: Net-(Q3-Pad1) -> Net-(D11-Pad2)
- Q3 pad 2: GND -> Net-(C73-Pad1)
- Q3 pad 3: Net-(Q3-Pad3) -> Net-(D11-Pad1)
- Q4 pad 1: Net-(D6-Pad2) -> Net-(Q4-Pad1)
- Q4 pad 2: Net-(C70-Pad1) -> Net-(Q4-Pad2)
- Q4 pad 3: Net-(D6-Pad1) -> Net-(Q4-Pad3)
- R10 pad 1: Net-(C37-Pad1) -> Net-(C42-Pad1)
- R10 pad 2: Net-(R10-Pad2) -> /7SegmentDriver/BrightnessPWM
- R11 pad 1: +5V -> Net-(D4-Pad1)
- R11 pad 2: /ControllerUIBoard/ATMEGA_RESET -> Net-(R11-Pad2)
- R12 pad 2: /RPiCM4/RPi_I2C1_SDA -> /RPiCM4/I2C1_SDA
- R13 pad 2: /RPiCM4/RPi_I2C0_SDA -> /RPiCM4/I2C0_SDA
- R14 pad 2: /RPiCM4/RPi_I2C1_SCL -> /RPiCM4/I2C1_SCL
- R15 pad 2: /RPiCM4/RPi_I2C0_SCL -> /RPiCM4/I2C0_SCL
- R16 pad 2: /ControllerUIBoard/DataEncoderDataOutC -> /RPiCM4/nRPIBOOT
- R17 pad 2: /ControllerUIBoard/DataEncoderDataOutD -> /RPiCM4/EEPROM_nWP
- R18 pad 2: /ControllerUIBoard/DataEncoderDataOutE -> /RPiCM4/BT_nDisable
- R19 pad 2: /ControllerUIBoard/DataEncoderDataAvailable -> /RPiCM4/WL_nDisable
- R20 pad 1: +5V -> Net-(R20-Pad1)
- R20 pad 2: /ControllerUIBoard/ButtonA2GND -> Net-(C54-Pad1)
- R25 pad 1: Net-(R25-Pad1) -> GND
- R25 pad 2: GND -> /ControllerUIBoard/5V_EN_OUT
- R26 pad 1: Net-(C60-Pad1) -> Net-(C63-Pad1)
- R28 pad 1: Net-(C60-Pad1) -> GND
- R28 pad 2: Net-(Q3-Pad1) -> /PowerSupply/PWR_ENABLE
- R29 pad 1: Net-(Q3-Pad1) -> Net-(C63-Pad1)
- R29 pad 2: GND -> Net-(Q2-Pad1)
- R30 pad 1: Net-(D6-Pad1) -> Net-(Q2-Pad1)
- R30 pad 2: Net-(D6-Pad2) -> GND
- R31 pad 1: Net-(D6-Pad2) -> Net-(D11-Pad1)
- R31 pad 2: Net-(Q3-Pad3) -> Net-(D11-Pad2)
- U1 pad 5: /RTC/RPi_I2C0_SDA -> /RPiCM4/I2C0_SDA
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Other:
- board size 132.1 x 67.9 mm -> 132 x 68.5 mm

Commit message: - erster Stand für Abmessungen
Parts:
- removed H5, H6: MountingHole, MountingHole:MountingHole_4mm
- removed H9: MountingHole, MountingHole:MountingHole_8.4mm_M8
- moved C51 82.0 mm to (-22.4, 172.1)
- moved C52 82.0 mm to (-35.4, 184.9)
- moved C53 82.0 mm to (-23.0, 175.3)
- moved C56 82.0 mm to (-9.16, 170.8)
- moved C57 82.0 mm to (-40.4, 185.1)
- moved C58 82.0 mm to (-17.4, 176.1)
- moved C59 82.0 mm to (-30.6, 181.4)
- moved C61 82.0 mm to (-13.6, 173.6)
- moved C62 82.0 mm to (-25.6, 180.0)
- moved C63 82.0 mm to (-11.7, 165.8)
- moved C64 82.0 mm to (-28.0, 176.5)
- moved C65 82.0 mm to (-16.6, 162.0)
- moved C66 82.0 mm to (-21.4, 178.0)
- moved C67 82.0 mm to (-25.8, 182.8)
- moved C68 82.0 mm to (-30.9, 184.9)
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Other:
- outline, holes or cut-outs redrawn
- board text added: "LOCK"
- board text added: "Ø2,5"
- board text added: "Ø3,2"
- board text added: "Ø4,0"
- board text added: "Ø8,0"
- board text removed: "For lock implementation"
